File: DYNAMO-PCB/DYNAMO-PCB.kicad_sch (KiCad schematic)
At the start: 6 parts, among them J1 USB_C_Receptacle, J2 USB3_A, J3 Conn_01x03_Pin, SW1 SW_SPST

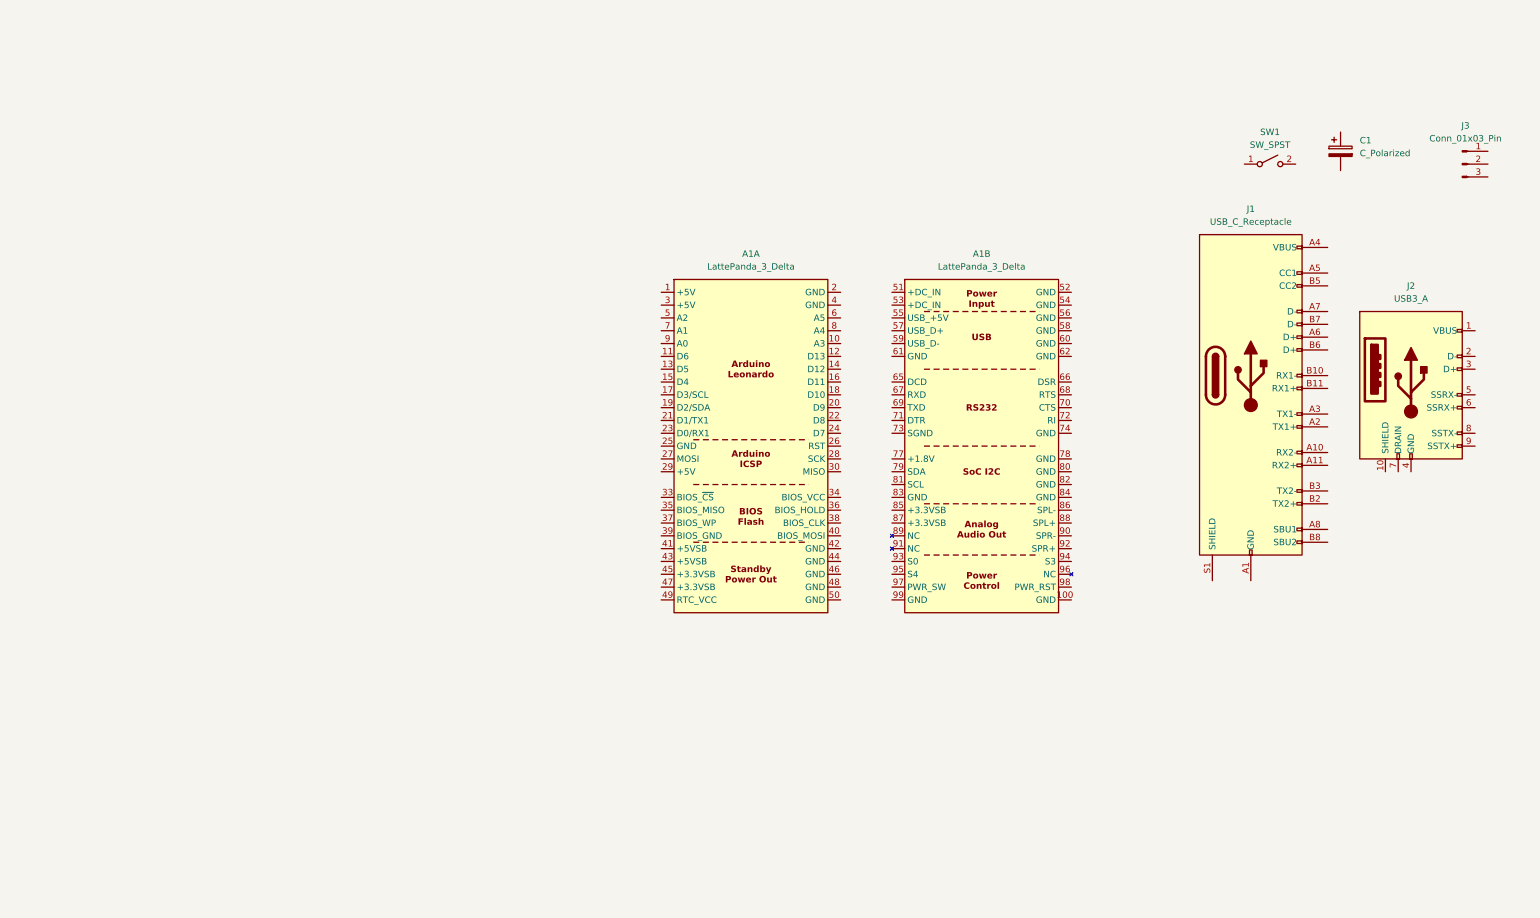
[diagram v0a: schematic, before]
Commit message: on/off switch
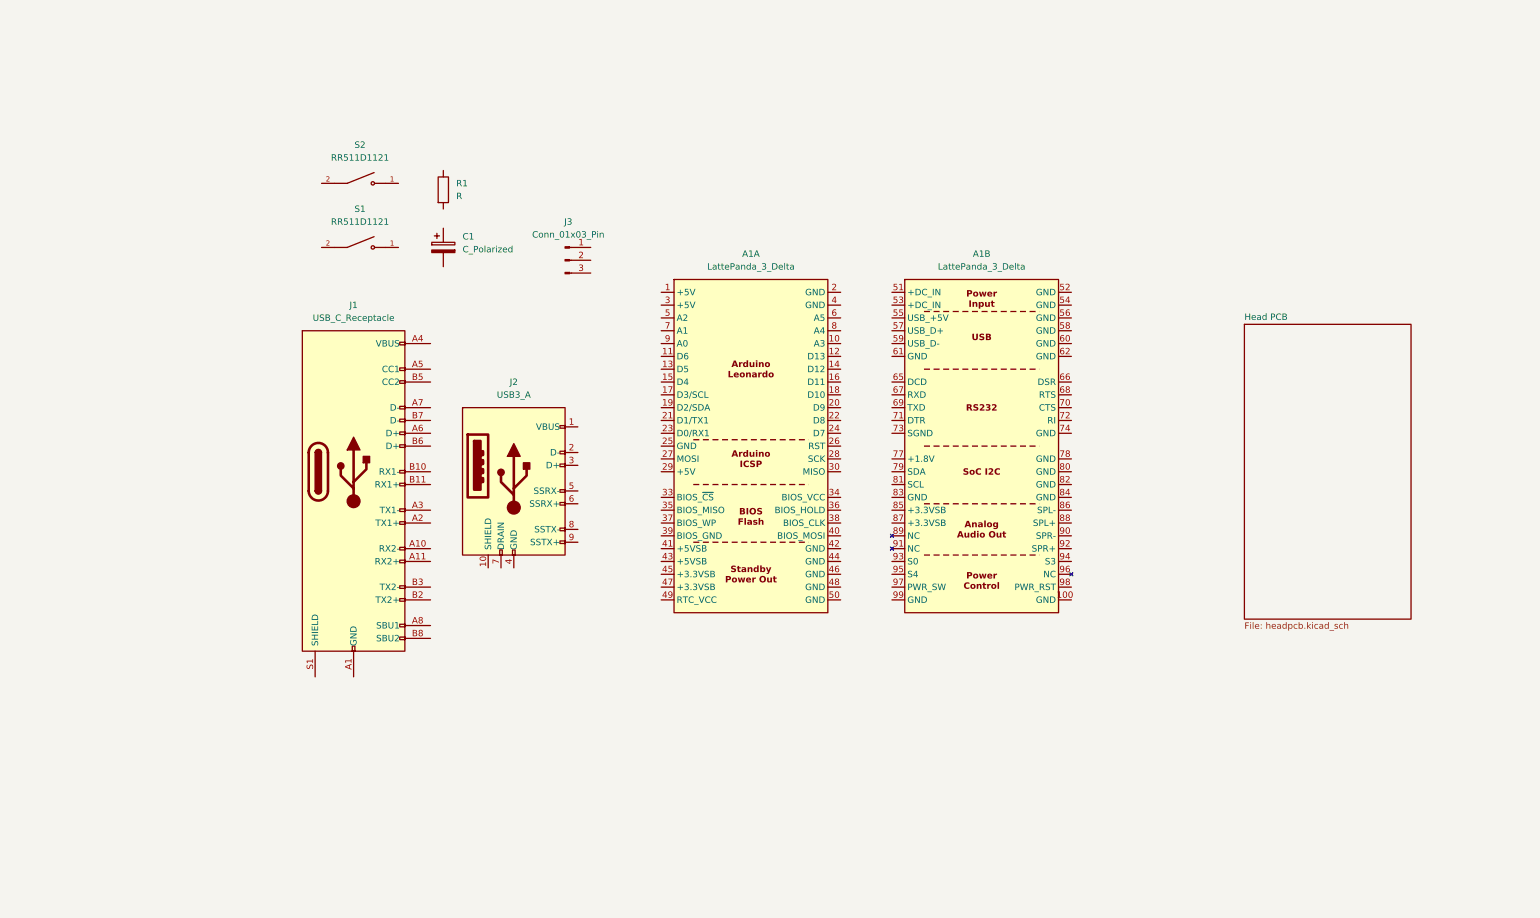
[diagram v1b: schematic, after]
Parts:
- removed SW1: SW_SPST, symbol Switch:SW_SPST
- added R1: R, symbol Device:R
- added S1, S2: RR511D1121, RR511D1121:E-SWITCH_RR511D1121, symbol RR511D1121:RR511D1121
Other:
- added sheet Head PCB (headpcb.kicad_sch)
- moved on the sheet: C1, J1, J2, J3

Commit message: 692122030100
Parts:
- removed J1: USB_C_Receptacle, symbol Connector:USB_C_Receptacle
- added J17, J18, J19, J20, J21, J22, J23, J24, J25: USB3_A, 692122030100:692122030100, symbol Connector:USB3_A
- added J26, J27, J28, J29, J30: USB_C_Receptacle_USB2.0_16P, Connector_USB:USB_C_Receptacle_GCT_USB4105-xx-A_16P_TopMnt_Horizontal, symbol Connector:USB_C_Receptacle_USB2.0_16P
- J2: footprint (none) -> 692122030100:692122030100
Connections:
- new net: J28.A1 (GND), J28.A12 (GND), J28.B1 (GND), J28.B12 (GND)
- new net: J28.A4 (VBUS), J28.A9 (VBUS), J28.B4 (VBUS), J28.B9 (VBUS)
- new net: J30.A1 (GND), J30.A12 (GND), J30.B1 (GND), J30.B12 (GND)
- new net: J30.A4 (VBUS), J30.A9 (VBUS), J30.B4 (VBUS), J30.B9 (VBUS)
- new net: J27.A1 (GND), J27.A12 (GND), J27.B1 (GND), J27.B12 (GND)
- new net: J27.A4 (VBUS), J27.A9 (VBUS), J27.B4 (VBUS), J27.B9 (VBUS)
- new net: J26.A1 (GND), J26.A12 (GND), J26.B1 (GND), J26.B12 (GND)
- new net: J26.A4 (VBUS), J26.A9 (VBUS), J26.B4 (VBUS), J26.B9 (VBUS)
- new net: J29.A1 (GND), J29.A12 (GND), J29.B1 (GND), J29.B12 (GND)
- new net: J29.A4 (VBUS), J29.A9 (VBUS), J29.B4 (VBUS), J29.B9 (VBUS)
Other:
- moved on the sheet: A1A, A1B, C1, J2, J3, R1, S1, S2

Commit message: footprint assignments
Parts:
- C1: footprint (none) -> Capacitor_THT:CP_Radial_D10.0mm_P5.00mm
- J3: footprint (none) -> Connector_PinHeader_2.54mm:PinHeader_1x03_P2.54mm_Vertical
- R1: footprint (none) -> Resistor_THT:R_Axial_DIN0309_L9.0mm_D3.2mm_P12.70mm_Horizontal
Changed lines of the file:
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@@
 			)
 		)
-		(property "Footprint" ""
+		(property "Footprint" "Connector_PinHeader_2.54mm:PinHeader_1x03_P2.54mm_Vertical"
 			(at 271.78 44.45 0)
 			(effects
@@
 			)
 		)
-		(property "Footprint" ""
+		(property "Footprint" "Capacitor_THT:CP_Radial_D10.0mm_P5.00mm"
 			(at 248.6152 45.72 0)
 			(effects
@@
 			)
 		)
-		(property "Footprint" ""
+		(property "Footprint" "Resistor_THT:R_Axial_DIN0309_L9.0mm_D3.2mm_P12.70mm_Horizontal"
 			(at 245.872 30.48 90)
 			(effects

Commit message: schematic wip
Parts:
- added C2, C3, C4, C5, C6, C7: C_Polarized, Capacitor_THT:CP_Radial_D10.0mm_P5.00mm, symbol Device:C_Polarized
- added J13: Conn_01x02_Pin, Connector_PinHeader_2.54mm:PinHeader_1x02_P2.54mm_Vertical, symbol Connector:Conn_01x02_Pin
- added J32: USB3_A, 692122030100:692122030100, symbol Connector:USB3_A
- added R2, R3: R, Resistor_THT:R_Axial_DIN0309_L9.0mm_D3.2mm_P12.70mm_Horizontal, symbol Device:R
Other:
- moved on the sheet: A1A, A1B, C1, J17, J18, J19, J2, J20, J21, J22, J23, J24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

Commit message: schematic wip
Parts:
- removed C2, C3, C4, C5, C6, C7: C_Polarized, Capacitor_THT:CP_Radial_D10.0mm_P5.00mm, symbol Device:C_Polarized
- removed J19, J20: USB3_A, 692122030100:692122030100, symbol Connector:USB3_A
- removed J26, J27, J28, J30: USB_C_Receptacle_USB2.0_16P, Connector_USB:USB_C_Receptacle_GCT_USB4105-xx-A_16P_TopMnt_Horizontal, symbol Connector:USB_C_Receptacle_USB2.0_16P
- removed R2, R3: R, Resistor_THT:R_Axial_DIN0309_L9.0mm_D3.2mm_P12.70mm_Horizontal, symbol Device:R
- removed S1, S2: RR511D1121, RR511D1121:E-SWITCH_RR511D1121, symbol RR511D1121:RR511D1121
- added J1: HDMI_A, Connector_Video:HDMI_A_Molex_208658-1001_Horizontal, symbol Connector:HDMI_A
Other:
- added sheet HDMI adapter (hdmiadapter.kicad_sch)
- added sheet Power Distribution (powerdistrib.kicad_sch)
- added sheet USB Hub (usbhhub.kicad_sch)
- moved on the sheet: C1, J13, J17, J18, J2, J21, J22, J23, J24, J25, J29, J3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

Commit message: second hdmi port on subsheet
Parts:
- removed J1: HDMI_A, Connector_Video:HDMI_A_Molex_208658-1001_Horizontal, symbol Connector:HDMI_A
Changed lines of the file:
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@@
-	)
-	(symbol
-		(lib_id "Connector:HDMI_A")
-		(at 43.18 27.94 90)
-		(unit 1)
-		(exclude_from_sim no)
-		(in_bom yes)
-		(on_board yes)
-		(dnp no)
-		(fields_autoplaced yes)
-		(property "Reference" "J1"
-			(at 43.18 12.7 90)
-			(effects
-				(font
-					(size 1.27 1.27)
-				)
-			)
-		)
-		(property "Value" "HDMI_A"
-			(at 43.18 15.24 90)
-			(effects
-				(font
-					(size 1.27 1.27)
-				)
-			)
-		)
-		(property "Footprint" "Connector_Video:HDMI_A_Molex_208658-1001_Horizontal"
-			(at 43.18 27.305 0)
-			(effects
-				(font
-					(size 1.27 1.27)
-				)
-				(hide yes)
-			)
-		)
-		(property "Datasheet" "https://en.wikipedia.org/wiki/HDMI"
-			(at 43.18 27.305 0)
-			(effects
-				(font
-					(size 1.27 1.27)
-				)
-				(hide yes)
-			)
-		)
-		(property "Description" "HDMI type A connector"
-			(at 43.18 27.94 0)
-			(effects
-				(font
-					(size 1.27 1.27)
-				)
-				(hide yes)
-			)
-		)
-		(pin "6"
-		)
-		(pin "9"
-		)
-		(pin "12"
-		)
-		(pin "16"
-		)
-		(pin "14"
-		)
-		(pin "19"
-		)
-		(pin "1"
-		)
-		(pin "3"
-		)
-		(pin "4"
-		)
-		(pin "7"
-		)
-		(pin "10"
-		)
-		(pin "13"
-		)
-		(pin "15"
-		)
-		(pin "17"
-		)
-		(pin "5"
-		)
-		(pin "8"
-		)
-		(pin "18"
-		)
-		(pin "2"
-		)
-		(pin "11"
-		)
-		(pin "SH"
-		)
-		(instances
-			(project ""
-				(path "/2ca9dd43-411d-4cc5-8a4b-ed00d72bae91"
-					(reference "J1")
-					(unit 1)
-				)
-			)
-		)
 	)
 	(symbol

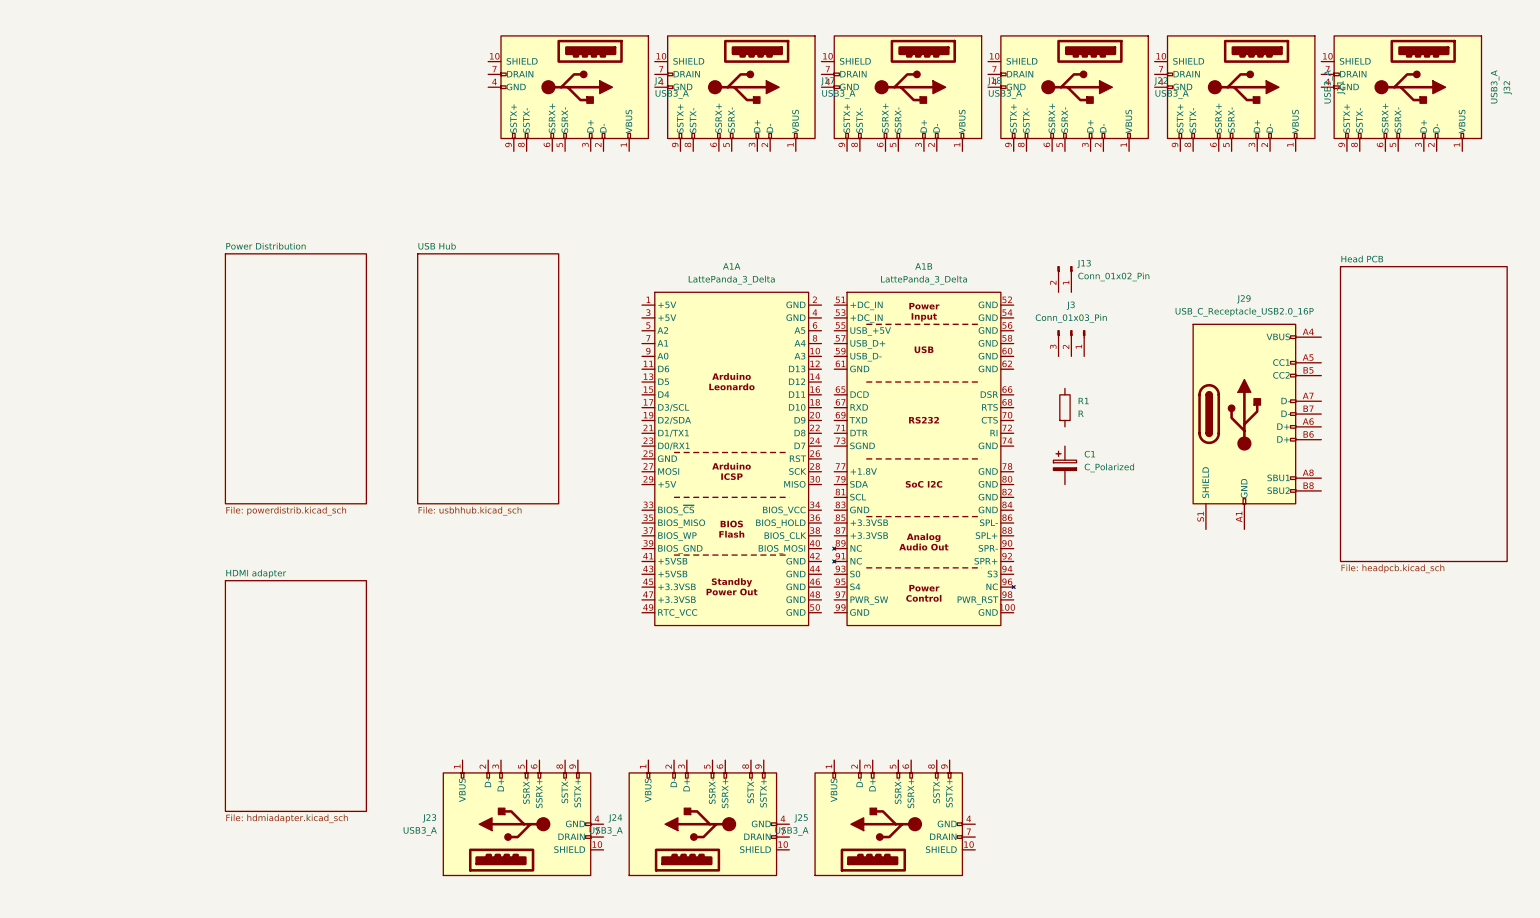
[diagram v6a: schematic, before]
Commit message: removed unncessary ic
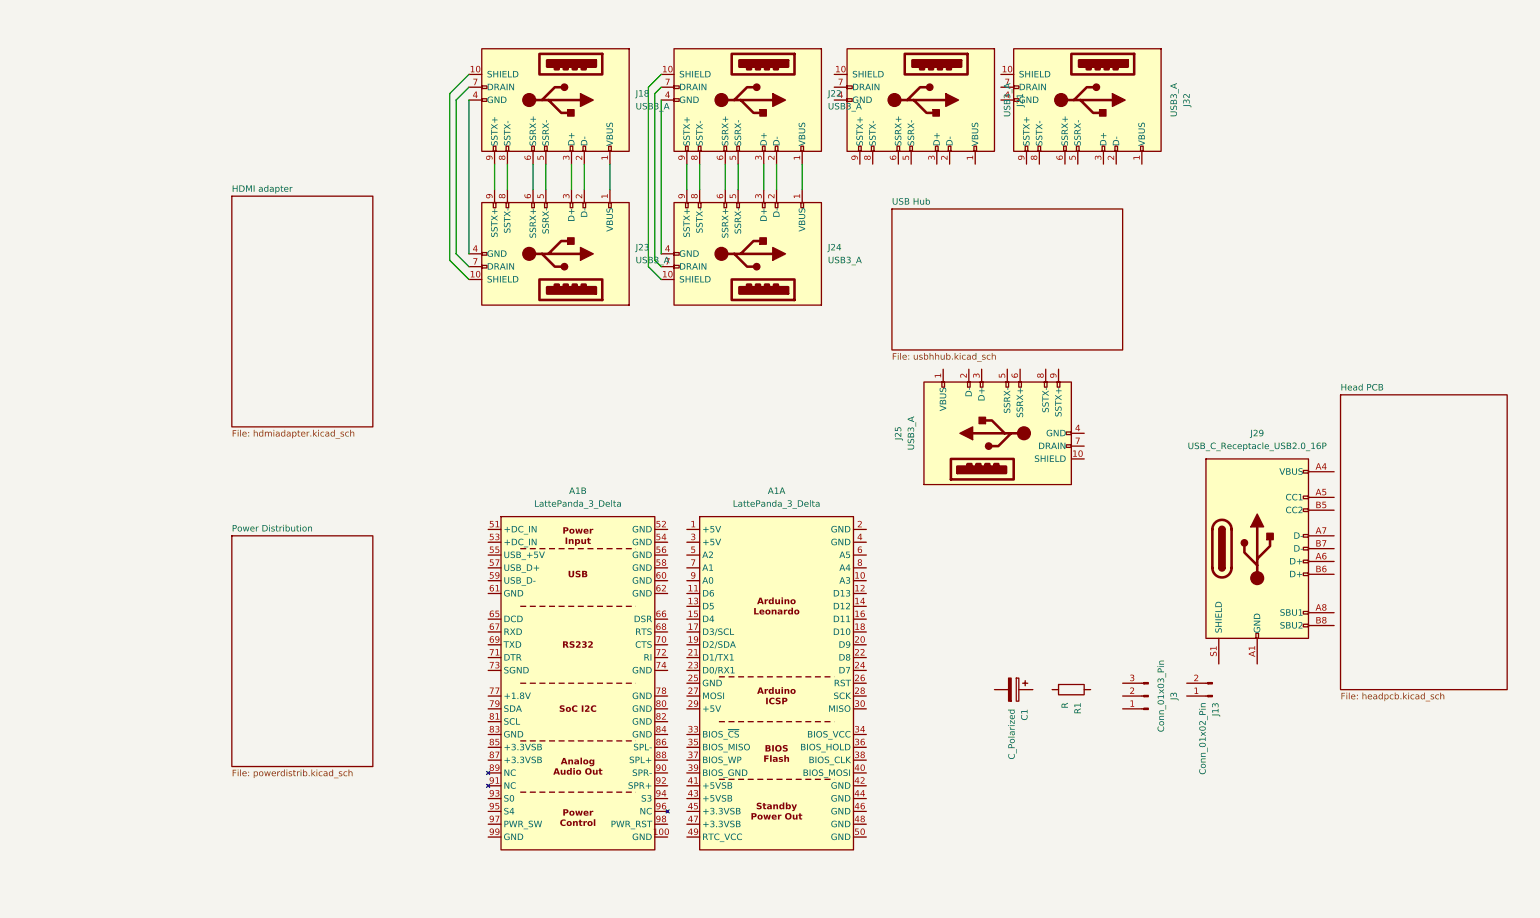
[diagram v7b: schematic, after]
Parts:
- removed J17, J2: USB3_A, 692122030100:692122030100, symbol Connector:USB3_A
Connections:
- net at J24.1 (VBUS): now also J22.1 (VBUS)
- net at J24.10 (SHIELD): now also J22.10 (SHIELD)
- net at J24.2 (D-): now also J22.2 (D-)
- net at J24.3 (D+): now also J22.3 (D+)
- net at J24.4 (GND): now also J22.4 (GND)
- net at J24.5 (SSRX-): now also J22.5 (SSRX-)
- net at J24.6 (SSRX+): now also J22.6 (SSRX+)
- net at J24.7 (DRAIN): now also J22.7 (DRAIN)
- net at J24.8 (SSTX-): now also J22.8 (SSTX-)
- net at J24.9 (SSTX+): now also J22.9 (SSTX+)
- net at J18.1 (VBUS): now also J23.1 (VBUS)
- net at J18.10 (SHIELD): now also J23.10 (SHIELD)
- net at J18.2 (D-): now also J23.2 (D-)
- net at J18.3 (D+): now also J23.3 (D+)
- net at J18.4 (GND): now also J23.4 (GND)
- net at J18.5 (SSRX-): now also J23.5 (SSRX-)
- net at J18.6 (SSRX+): now also J23.6 (SSRX+)
- net at J18.7 (DRAIN): now also J23.7 (DRAIN)
- net at J18.8 (SSTX-): now also J23.8 (SSTX-)
- net at J18.9 (SSTX+): now also J23.9 (SSTX+)
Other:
- moved on the sheet: A1A, A1B, C1, J13, J18, J21, J22, J23, J24, J25, J29, J3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

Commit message: removed usb7206
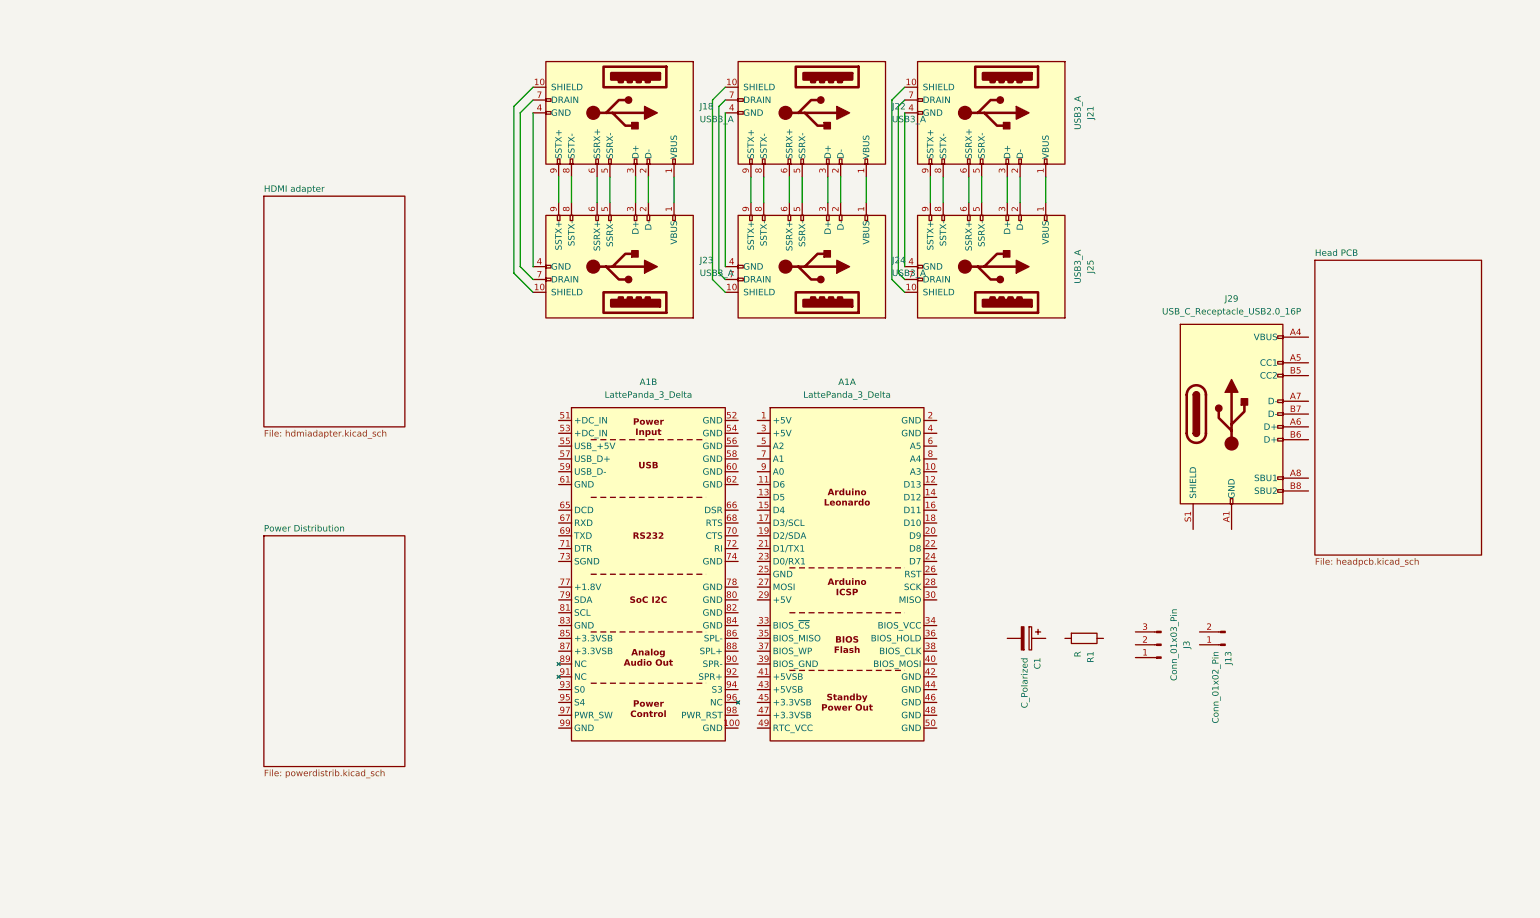
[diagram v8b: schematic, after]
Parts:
- removed J32: USB3_A, 692122030100:692122030100, symbol Connector:USB3_A
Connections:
- net at J21.1 (VBUS): now also J25.1 (VBUS)
- net at J21.10 (SHIELD): now also J25.10 (SHIELD)
- net at J21.2 (D-): now also J25.2 (D-)
- net at J21.3 (D+): now also J25.3 (D+)
- net at J21.4 (GND): now also J25.4 (GND)
- net at J21.5 (SSRX-): now also J25.5 (SSRX-)
- net at J21.6 (SSRX+): now also J25.6 (SSRX+)
- net at J21.7 (DRAIN): now also J25.7 (DRAIN)
- net at J21.8 (SSTX-): now also J25.8 (SSTX-)
- net at J21.9 (SSTX+): now also J25.9 (SSTX+)
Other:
- removed sheet USB Hub
- moved on the sheet: A1A, A1B, C1, J13, J18, J21, J22, J23, J24, J25, J29, J3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
